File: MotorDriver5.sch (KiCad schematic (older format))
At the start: 27 parts, among them J26 PH1RA-08-UA, U53 DRV8312DDWR, U54 MIC2090-2YM5-TR

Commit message: PVT
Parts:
- removed C237: 1u, Capacitor-Chip:C_CHIP_1005_Hand_NoSilk, symbol passive:C
- C217: renamed from C225; footprint Capacitor-Chip:C_CHIP_1608_Reflow -> Capacitor-Chip:C_CHIP_1005_Hand_NoSilk; PartName GRM188R61E105KA12D -> TMK105BJ105MV-F
- C218: renamed from C226; footprint Capacitor-Chip:C_CHIP_1608_Reflow -> Capacitor-Chip:C_CHIP_1005_Hand_NoSilk; PartName GRM188R61E105KA12D -> TMK105BJ105MV-F
- C219: renamed from C227; footprint Capacitor-Chip:C_CHIP_1608_Reflow -> Capacitor-Chip:C_CHIP_1005_Hand_NoSilk; PartName GRM188R61E105KA12D -> TMK105BJ105MV-F
- C220: renamed from C228; footprint Capacitor-Chip:C_CHIP_1608_Reflow -> Capacitor-Chip:C_CHIP_1005_Hand_NoSilk; PartName GRM188R61E105KA12D -> TMK105BJ105MV-F
- C228: renamed from C236; PartName C1005X5R1V105K050BE -> TMK105BJ105MV-F
- R116: renamed from R131; value 10m -> 20m; PartName ERJ-8CWJR010V -> ERJ-8CWJR020V
- renumbered C229 to C221, C230 to C222, C231 to C223, C232 to C224, C233 to C225, C234 to C226, C235 to C227, L25 to L21, L26 to L22, L27 to L23, R129 to R114, R130 to R115, R132 to R117, R133 to R118, RA30 to RA31, RA31 to RA32, RA32 to RA33, U53 to U50, U54 to U51

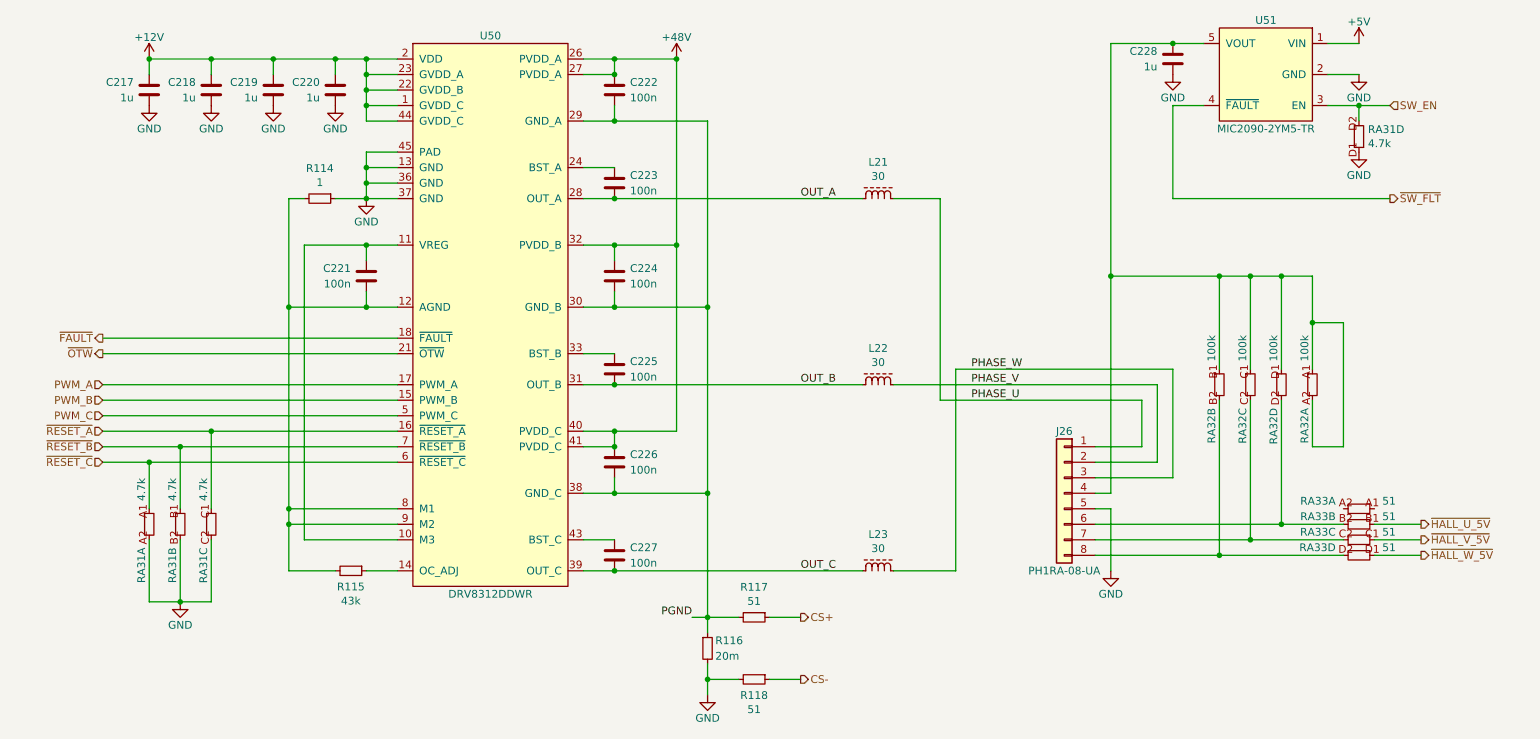
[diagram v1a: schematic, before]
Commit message: SBUにTVSダイオードを追加
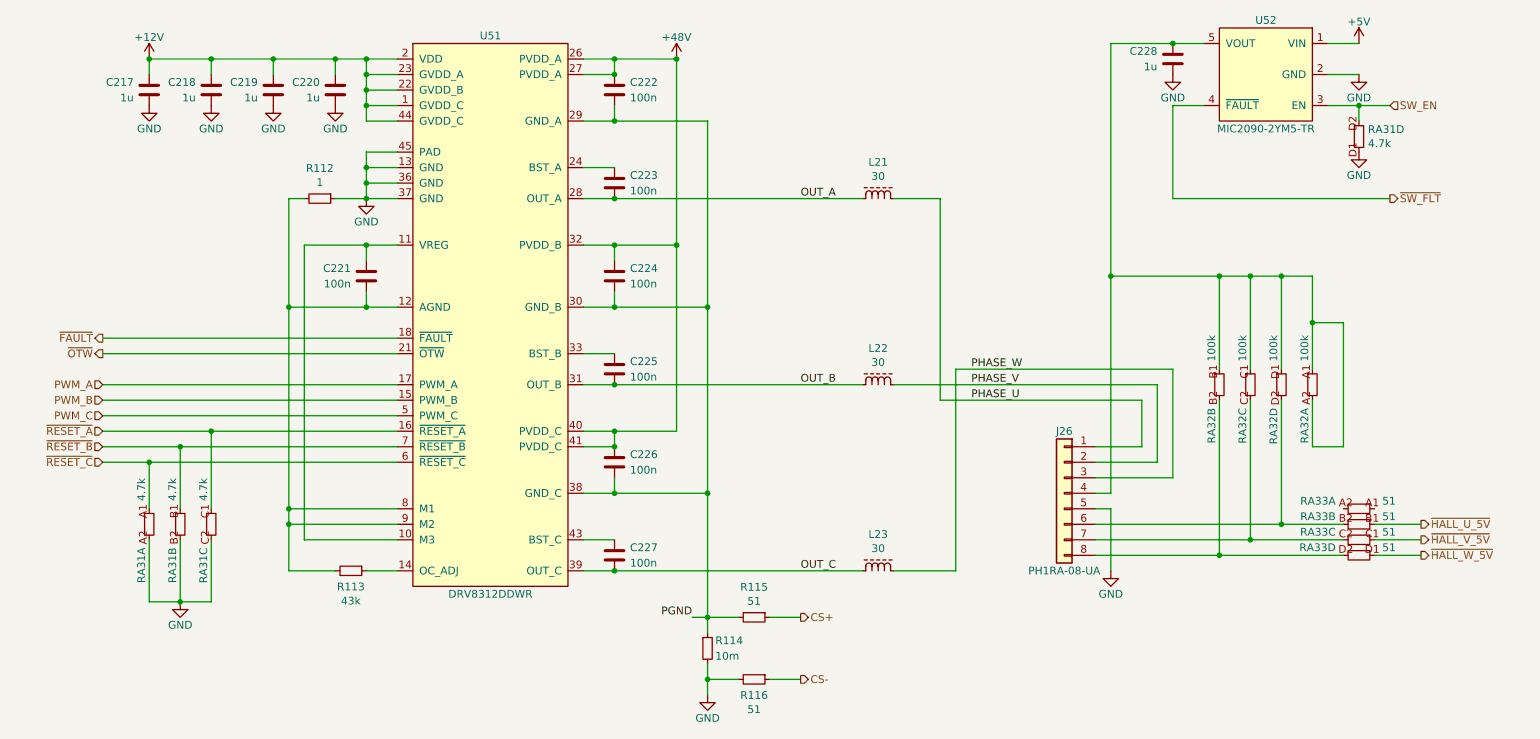
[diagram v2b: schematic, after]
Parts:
- R114: renamed from R116; value 20m -> 10m; PartName ERJ-8CWJR020V -> ERJ-8CWJR010V
- renumbered R114 to R112, R115 to R113, R117 to R115, R118 to R116, U50 to U51, U51 to U52
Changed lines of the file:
@@
 AR Path="/5F237486/5E63CE20" Ref="U?"  Part="1"
 AR Path="/5F259EEE/5E63CE20" Ref="U?"  Part="1"
-AR Path="/5F259FB4/5E63CE20" Ref="U50"  Part="1"
-F 0 "U50" H 4000 5450 50  0000 C CNN
+AR Path="/5F259FB4/5E63CE20" Ref="U51"  Part="1"
+F 0 "U51" H 4000 5450 50  0000 C CNN
 F 1 "DRV8312DDWR" H 4000 1850 50  0000 C CNN
 F 2 "IC-SOP:HTSSOP44-W6.1_EP4.31x8.26" H 4000 3600 50  0001 C CNN
@@
 AR Path="/5F237486/5E63CF10" Ref="R?"  Part="1"
 AR Path="/5F259EEE/5E63CF10" Ref="R?"  Part="1"
-AR Path="/5F259FB4/5E63CF10" Ref="R114"  Part="1"
-F 0 "R114" V 2705 2800 50  0000 C CNN
+AR Path="/5F259FB4/5E63CF10" Ref="R112"  Part="1"
+F 0 "R112" V 2705 2800 50  0000 C CNN
 F 1 "1" V 2796 2800 50  0000 C CNN
 F 2 "Resistor-Chip:R_CHIP_1005_Hand_NoSilk" V 2950 2700 50  0001 C CNN
@@
 AR Path="/5F237486/5E63CF1A" Ref="R?"  Part="1"
 AR Path="/5F259EEE/5E63CF1A" Ref="R?"  Part="1"
-AR Path="/5F259FB4/5E63CF1A" Ref="R115"  Part="1"
-F 0 "R115" V 3203 5200 50  0000 C CNN
+AR Path="/5F259FB4/5E63CF1A" Ref="R113"  Part="1"
+F 0 "R113" V 3203 5200 50  0000 C CNN
 F 1 "43k" V 3294 5200 50  0000 C CNN
 F 2 "Resistor-Chip:R_CHIP_1005_Hand_NoSilk" V 3150 5100 50  0001 C CNN
@@
 	4800 2800 6400 2800
 $Comp
-L passive:R R116
+L passive:R R114
 U 1 1 5E6024FD
 P 5400 5700
-F 0 "R116" H 5450 5750 50  0000 L CNN
-F 1 "20m" H 5450 5650 50  0000 L CNN
+F 0 "R114" H 5450 5750 50  0000 L CNN
+F 1 "10m" H 5450 5650 50  0000 L CNN
 F 2 "Resistor-Chip:R_CHIP_3216_Reflow" V 5450 5600 50  0001 C CNN
 F 3 "" H 5450 5800 50  0001 C CNN
-F 4 "ERJ-8CWJR020V" H 5400 5700 50  0001 C CNN "PartName"
+F 4 "ERJ-8CWJR010V" H 5400 5700 50  0001 C CNN "PartName"
 	1    5400 5700
 	1    0    0    -1
@@
 P 5700 5900
 AR Path="/5E83D44B/5E5A106C" Ref="R?"  Part="1"
-AR Path="/5F259FB4/5E5A106C" Ref="R118"  Part="1"
-F 0 "R118" V 5803 5900 50  0000 C CNN
+AR Path="/5F259FB4/5E5A106C" Ref="R116"  Part="1"
+F 0 "R116" V 5803 5900 50  0000 C CNN
 F 1 "51" V 5894 5900 50  0000 C CNN
 F 2 "Resistor-Chip:R_CHIP_1005_Hand_NoSilk" V 5750 5800 50  0001 C CNN
@@
 P 5700 5500
 AR Path="/5E83D44B/5E5A1072" Ref="R?"  Part="1"
-AR Path="/5F259FB4/5E5A1072" Ref="R117"  Part="1"
-F 0 "R117" V 5505 5500 50  0000 C CNN
+AR Path="/5F259FB4/5E5A1072" Ref="R115"  Part="1"
+F 0 "R115" V 5505 5500 50  0000 C CNN
 F 1 "51" V 5596 5500 50  0000 C CNN
 F 2 "Resistor-Chip:R_CHIP_1005_Hand_NoSilk" V 5750 5400 50  0001 C CNN
@@
 AR Path="/5F259EEE/5F232DE7" Ref="U?"  Part="1"
 AR Path="/5F259F40/5F232DE7" Ref="U?"  Part="1"
-AR Path="/5F259FB4/5F232DE7" Ref="U51"  Part="1"
-F 0 "U51" H 9000 2350 50  0000 C CNN
+AR Path="/5F259FB4/5F232DE7" Ref="U52"  Part="1"
+F 0 "U52" H 9000 2350 50  0000 C CNN
 F 1 "MIC2090-2YM5-TR" H 9000 1650 50  0000 C CNN
 F 2 "IC-SOT:SOT23-5" H 9000 2000 50  0001 C CNN
